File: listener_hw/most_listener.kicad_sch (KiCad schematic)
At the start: 121 parts, among them J1 1-1394640-1, J2 ANALYSER, J3 I2S, J4 VBAT_IN, J5 PLR135/T10, J6 PLT133/T10W, J7 RCA 75R, M1 Tang Nano 20K, M2 ESP32-DevKitC-VIE, U1 74LVC1G34, U10 TPS2553DBVR, U11 74LVC1G123, U12 DIR9001, U13 SRC4192, U14 LP5907MFX-3.3, U2 74LVC1G157, U3 74LVC1G125, U4 74LVC1G123, U5 TPS7B8133DRV, U6 LMR38020F, U7 Si514, U8 LP5907MFX-3.3, U9 74LVC1G79, X1 24.576MHz

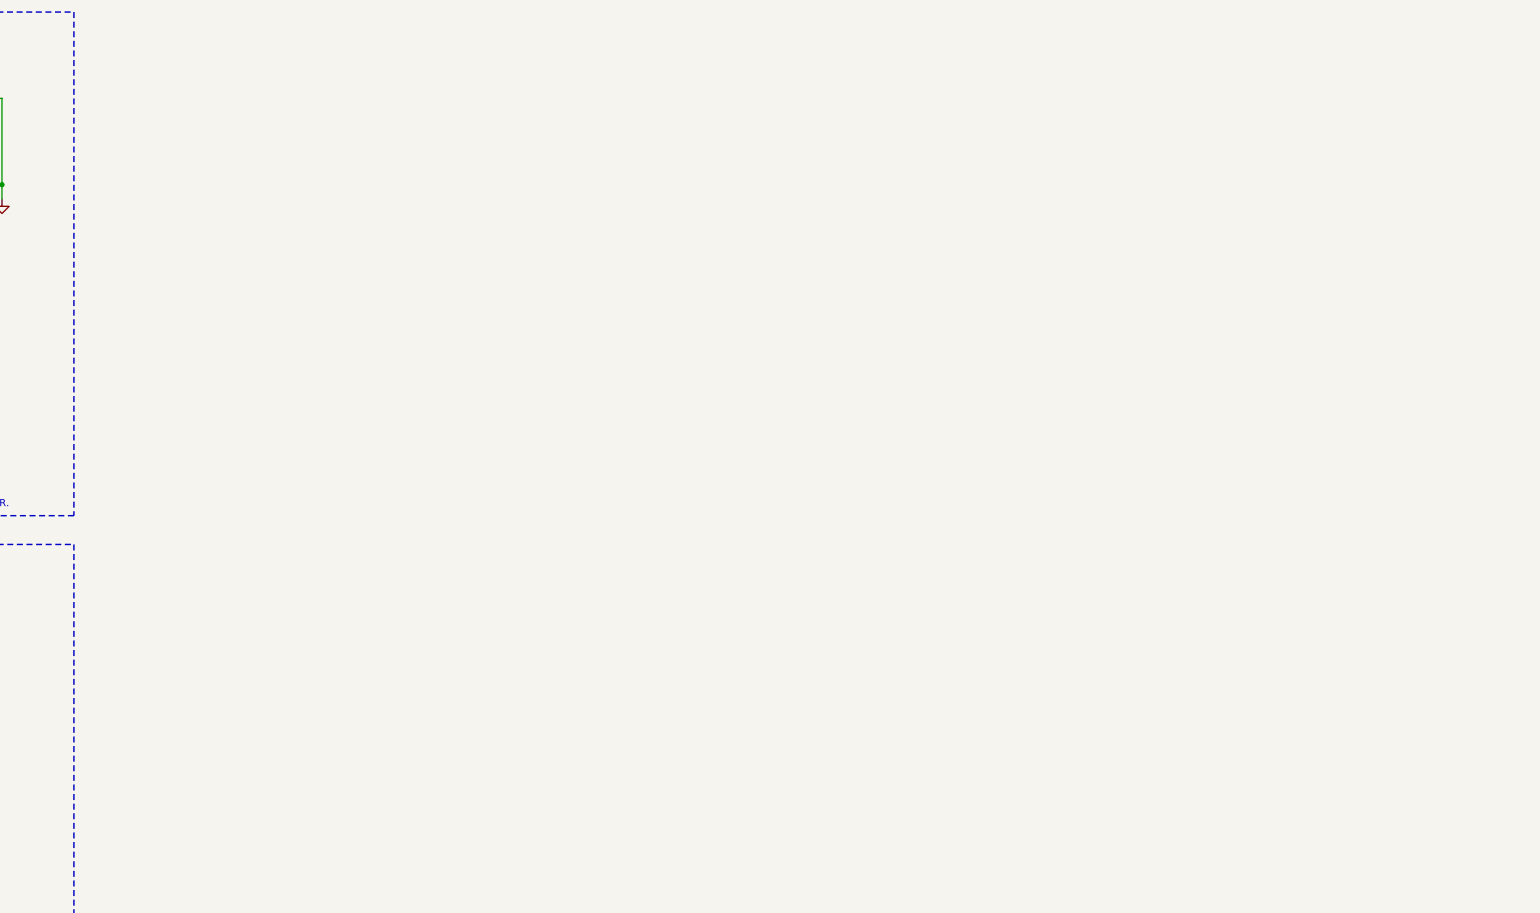
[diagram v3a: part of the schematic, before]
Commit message: Board: block 11, analog line out - PCM5102A on J3's stereo into the two RCA jacks placed by hand; footprints linked to the sheet
Sheet, block 11: U15 PCM5102A in hardware mode (FMT, FLT, DEMP low: I2S,
normal latency, no de-emphasis), SCK grounded so its PLL takes the clock from
BCK - three wires, the same I2S_BCLK_F / I2S_LRCK_F / I2S_DOUT_F that feed
J3 (64 Fs, 32-bit slots). XSMT from LOCK: muted while the ring is not locked
and while the FPGA is unconfigured (R8 holds LOCK low), with the chip's
104-sample soft ramp; no new FPGA pin, no gateware change. Outputs 2.1 Vrms
ground-centred through 470R + 2n2 C0G (TI SLAS859C Figure 33) to J8 (L) and
J9 (R), a PESD5V0S1BL at each jack as D4 at J7. U16, an LP5907, makes
3V3_DAC from 5V_SW; its output capacitance must stay within 10 uF (LP5907
data sheet), so AVDD gets 4.7 uF and CPVDD 2.2 uF instead of Figure 33's
10 uF each; LDOO 100n + 10u, flying cap and VNEG 2u2 each. Test points are
out of the BOM now (their footprints already said so). ERC clean.

Board: the placement the user reworked by hand since cddadba (the power
corner, block 9, J2/J3/U10 moved to the bottom middle, a fifth mounting hole
H5 at the top, two RCA jacks on the right edge copied from J7). The copies
became J9 (upper, right channel) and J8 (lower, left); block 11 sits in the
corner beside them, U15 turned so its analog pins face the jacks and its
digital pins face the I2S coming down from M2's pins. Every footprint now
carries its symbol's path and library name and single pins their
unconnected nets, the holes are board-only - DRC with --schematic-parity
finds no difference, so Update PCB from Schematic works from here. The
antenna keep-out is squared with M2 again. DRC: no error; the warnings are
silk, most of it in the hand-moved areas.

gen_listener_pcb.py writes the same links and parks parts its table does
not know beside the board instead of stopping. check_all.py's board step
also fails on any difference from the sheet. KiCad's local histor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
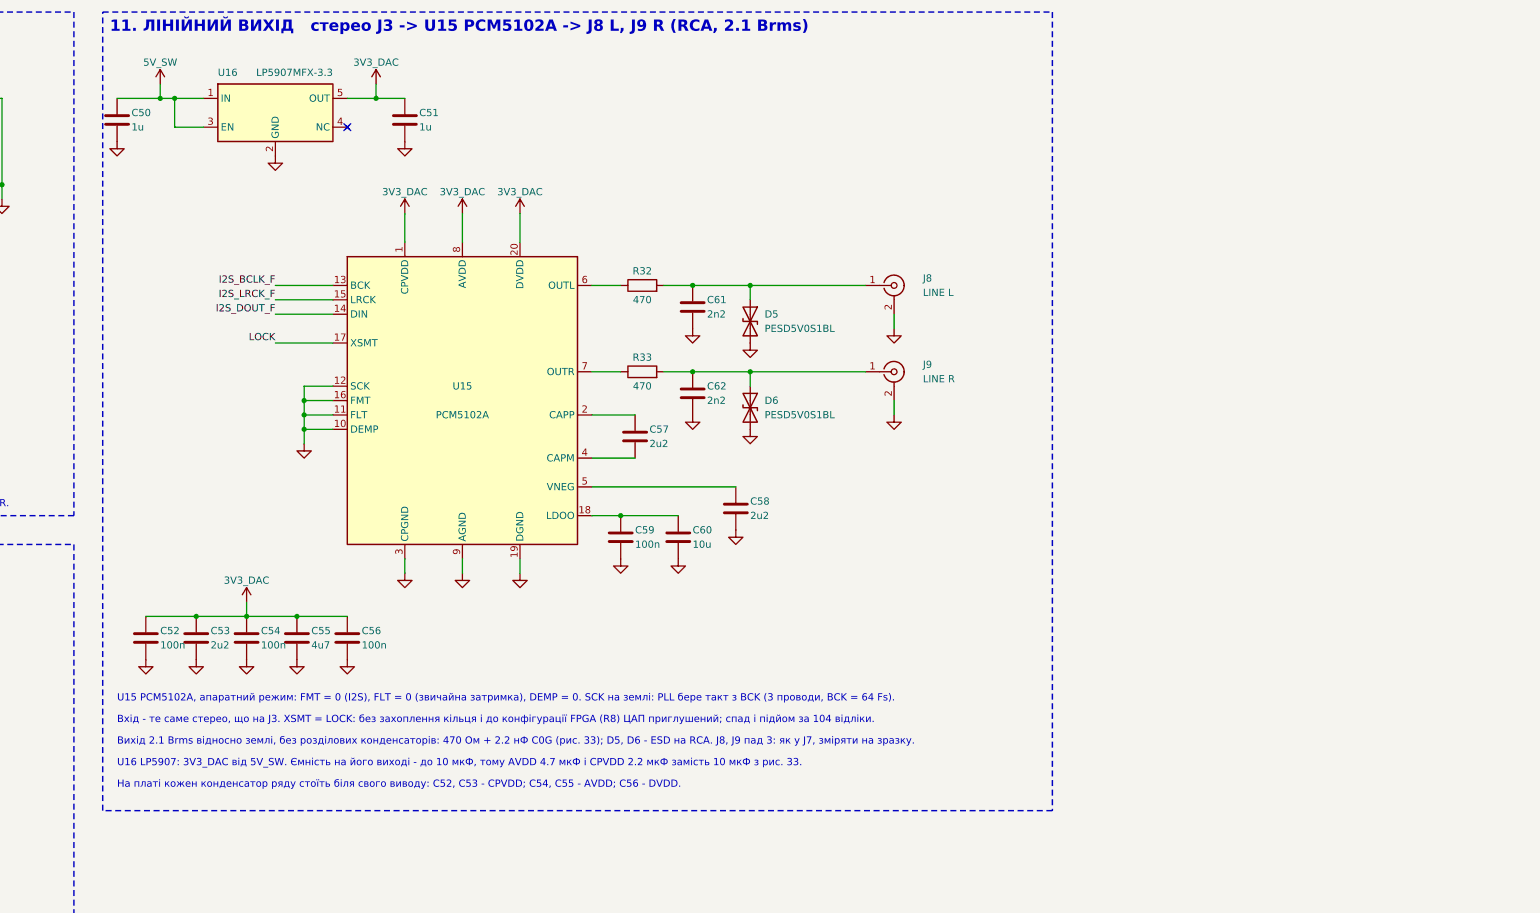
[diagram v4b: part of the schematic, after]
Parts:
- added C50, C51: 1u, Capacitor_SMD:C_0603_1608Metric, symbol Device:C
- added C52, C54, C56, C59: 100n, Capacitor_SMD:C_0603_1608Metric, symbol Device:C
- added C53, C57, C58: 2u2, Capacitor_SMD:C_0603_1608Metric, symbol Device:C
- added C55: 4u7, Capacitor_SMD:C_0805_2012Metric, symbol Device:C
- added C60: 10u, Capacitor_SMD:C_0805_2012Metric, symbol Device:C
- added C61, C62: 2n2, Capacitor_SMD:C_0603_1608Metric, symbol Device:C
- added D5, D6: PESD5V0S1BL, Diode_SMD:D_SOD-882, symbol Device:D_TVS
- added J8: LINE L, most_listener:BKL_0101153_RCA_RA, symbol Connector:Conn_Coaxial
- added J9: LINE R, most_listener:BKL_0101153_RCA_RA, symbol Connector:Conn_Coaxial
- added R32, R33: 470, Resistor_SMD:R_0603_1608Metric, symbol Device:R
- added U15: PCM5102A, Package_SO:TSSOP-20_4.4x6.5mm_P0.65mm, symbol most_listener:PCM5102A
- added U16: LP5907MFX-3.3, Package_TO_SOT_SMD:SOT-23-5, symbol most_listener:LP5907MFX-3.3
- TP1, TP2, TP3, TP4, TP5, TP6, TP7, TP8, TP9: now left out of the parts list
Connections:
- net 5V_SW: now also C50.1, U16.1 (IN), U16.3 (EN)
- net GND: now also C50.2, C51.2, C52.2, C53.2, C54.2, C55.2, C56.2, C58.2, C59.2, C60.2, C61.2, C62.2, D5.2 (A2), D6.2 (A2), J8.2 (Ext), J9.2 (Ext), U15.10 (DEMP), U15.11 (FLT), U15.12 (SCK), U15.16 (FMT), U15.19 (DGND), U15.3 (CPGND), U15.9 (AGND), U16.2 (GND)
- net I2S_BCLK_F: now also U15.13 (BCK)
- net I2S_DOUT_F: now also U15.14 (DIN)
- net I2S_LRCK_F: now also U15.15 (LRCK)
- net LOCK: now also U15.17 (XSMT)
- new net: C58.1, U15.5 (VNEG)
- new net: R33.1, U15.7 (OUTR)
- new net: C62.1, D6.1 (A1), J9.1 (In), R33.2
- new net: C59.1, C60.1, U15.18 (LDOO)
- new net: C61.1, D5.1 (A1), J8.1 (In), R32.2
- new net: C57.1, U15.2 (CAPP)
- new net: C57.2, U15.4 (CAPM)
- new net: R32.1, U15.6 (OUTL)
- new net 3V3_DAC: C51.1, C52.1, C53.1, C54.1, C55.1, C56.1, U15.1 (CPVDD), U15.20 (DVDD), U15.8 (AVDD), U16.5 (OUT)
- no-connect marks 62 -> 63
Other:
- note added: "11. ЛІНІЙНИЙ ВИХІД стерео J3 -> U15 PCM5102A -> J8 L, J9 R (RCA, 2.1 Вrms)"
- note added: "U15 PCM5102A, апаратний режим: FMT = 0 (I2S), FLT = 0 (звичайна затримка), DEMP = 0. SCK на землі: PLL бере такт з BCK (3 проводи, BCK = 64 Fs)."
- note added: "U16 LP5907: 3V3_DAC від 5V_SW. Ємність на його виході - до 10 мкФ, тому AVDD 4.7 мкФ і CPVDD 2.2 мкФ замість 10 мкФ з рис. 33."
- note added: "Вихід 2.1 Вrms відносно землі, без розділових конденсаторів: 470 Ом + 2.2 нФ C0G (рис. 33); D5, D6 - ESD на RCA. J8, J9 пад 3: як у J7, зміряти на зразку."
- note added: "Вхід - те саме стерео, що на J3. XSMT = LOCK: без захоплення кільця і до конфігурації FPGA (R8) ЦАП приглушений; спад і підйом за 104 відліки."
- note added: "На платі кожен конденсатор ряду стоїть біля свого виводу: C52, C53 - CPVDD; C54, C55 - AVDD; C56 - DVDD."

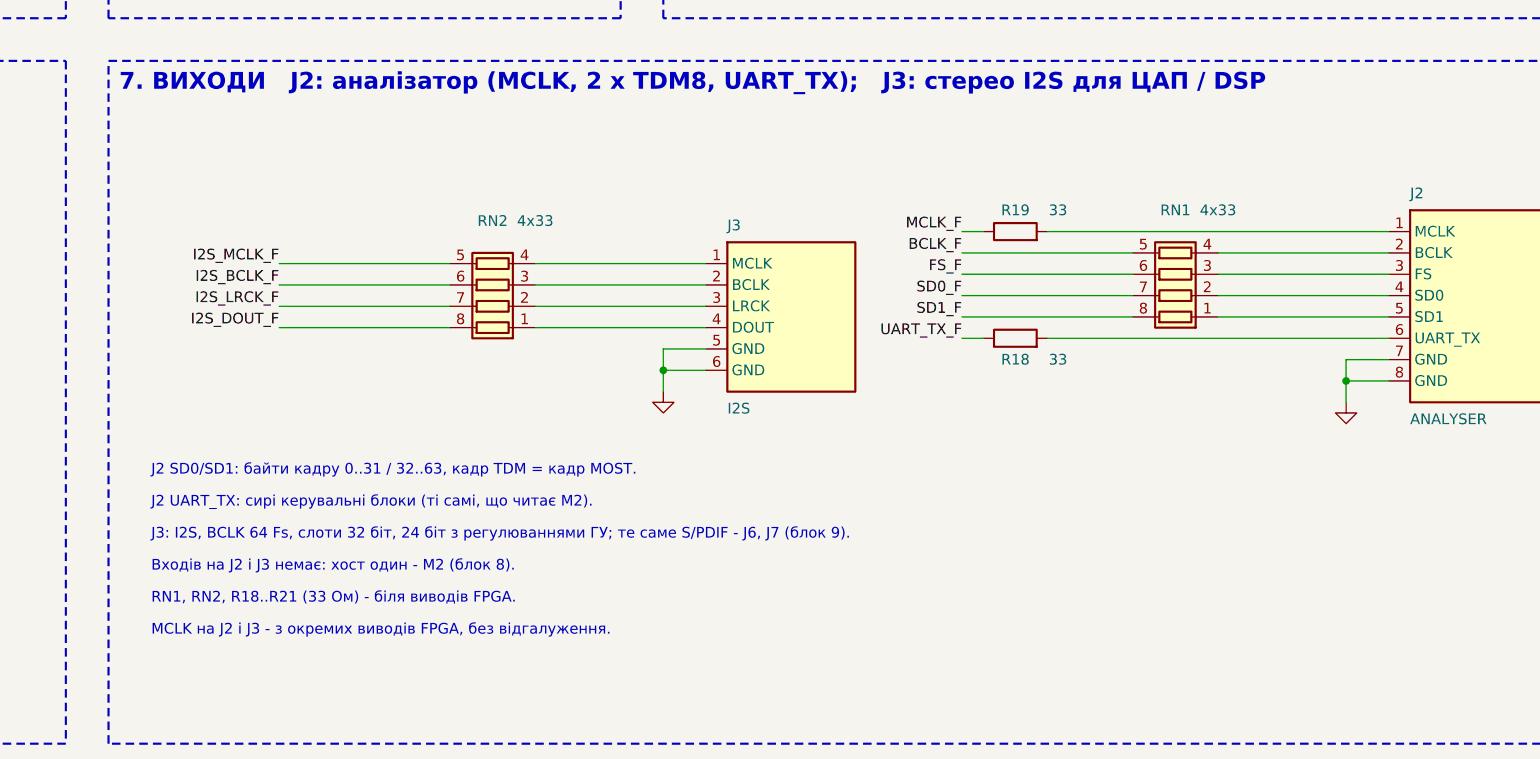
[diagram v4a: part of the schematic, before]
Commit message: Board: the user's regroup, reviewed - 33R singles under M1 at their FPGA pins, U14 back in block 9, block 9 turned to its jacks, the capacitor copies out
The user regrouped the board: M2 upright against M1 with both USB ends at
the top edge, every audio jack (TOSLINK in and out, coax, the two line-out
RCA) on the right edge, block 9 beside them, the host switch and the test
points in the bottom middle, a sixth mounting hole (H6) on the left edge.
Agreed after review and done here:

- Sheet: RN1 and RN2 (4 x 33R arrays) became single 0603 resistors, R34..R41,
  so each FPGA output to J2/J3 has its own. With R18..R21 they sit under M1,
  each beside its FPGA pin (source termination: MCLK, BCLK and TDM lines run
  to the headers and on through cables). The Tang Nano's footprint now keeps
  only its two socket rows as courtyard, so low parts may sit under the
  module standing on its 8.5 mm sockets; its outline stays on fab and silk.
  R20 had landed on M2's pins 37/38 (the seven DRC errors of the regroup);
  it sits at M1 pin 1 now. ERC clean.
- U14 with C48/C49 back in block 9: the clean 3V3_DA stays short, the long
  run is 5V_SW's.
- Block 9 re-laid for the jacks on the right edge: DIR9001 next to J5 with
  RXIN and its loop filter towards the jack, SRC4192 between it and the
  modules with its I2S outputs towards them, X1 at RCKI, FB3/C30 within 2 cm
  of J5 as the Everlight sheet asks, C31 by J6, the coax divider and D4 by J7.
- The three board-only copies each of C45 and C47 are gone: two 100 uF
  pairs are what the input needs; more only raises the inrush through F1.
- Both antenna keep-outs squared with M2 upright (the B.Cu one was half
  height); C61/D5 and C62/D6 moved up with J8/J9.

DRC: no error; 368 unconnected (not routed); the warnings are silk, for the
final silk pass. DRC with --schematic-parity: no difference. The board
generator's table lost RN1/RN2; a fresh layout parks the parts it does not
know beside the board and still matches the sheet.

Co-Au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
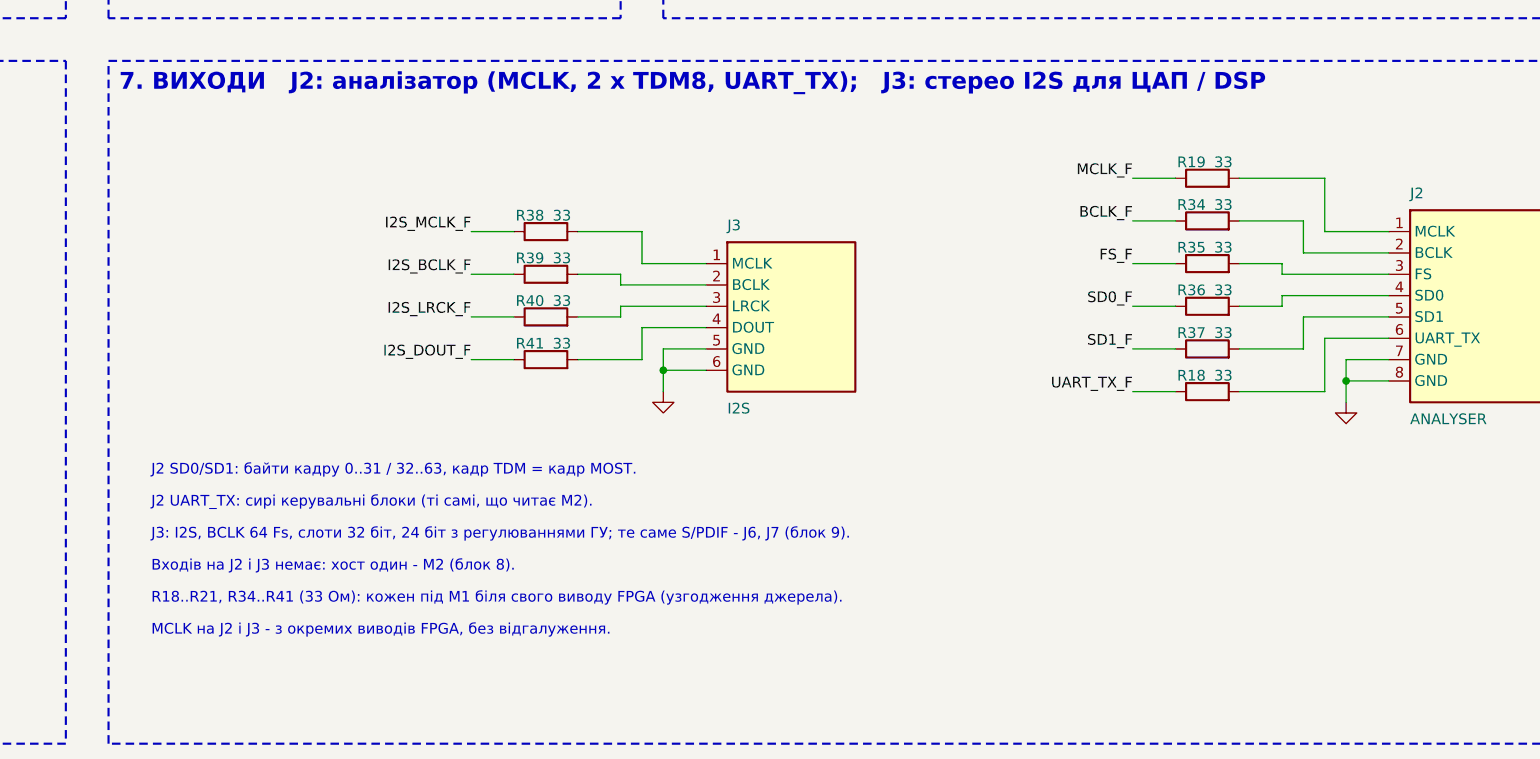
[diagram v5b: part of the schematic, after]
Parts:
- removed RN1, RN2: 4x33, Resistor_SMD:R_Array_Convex_4x0603, symbol Device:R_Pack04
- added R34, R35, R36, R37, R38, R39, R40, R41: 33, Resistor_SMD:R_0603_1608Metric, symbol Device:R
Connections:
- net BCLK_F: now also R34.1
- net FS_F: now also R35.1
- net I2S_BCLK_F: now also R39.1
- net I2S_DOUT_F: now also R41.1
- net I2S_LRCK_F: now also R40.1
- net I2S_MCLK_F: now also R38.1
- net SD0_F: now also R36.1
- net SD1_F: now also R37.1
- net at J3.1 (MCLK): now also R38.2
- net at J3.2 (BCLK): now also R39.2
- net at J3.3 (LRCK): now also R40.2
- net at J3.4 (DOUT): now also R41.2
- net at J2.5 (SD1): now also R37.2
- net at J2.4 (SD0): now also R36.2
- net at J2.3 (FS): now also R35.2
- net at J2.2 (BCLK): now also R34.2
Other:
- note added: "R18..R21, R34..R41 (33 Ом): кожен під M1 біля свого виводу FPGA (узгодження джерела)."
- note removed: "RN1, RN2, R18..R21 (33 Ом) - біля виводів FPGA."
- moved on the sheet: R18, R19

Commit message: Board: M1 and M2 left into the strip the user freed; resistors of M1's pins under it; signal test points above J1
The user cleared a vertical strip left of M1 and asked for the FPGA to move
into it, part of the resistors to go under the module, and the signal test
points to go to the left edge above the MOST header.

- The ring-logic column (U3, U9, R16) with R17 moved into the strip; M1
  followed it 6.7 mm to the left and M2 with M1, the two modules still side
  by side; the antenna keep-out moved with M2. The free space now lies
  between M2 and block 9, a channel for M2's signals to the right half.
- Under M1, each beside its pin, as before for J2/J3's 33R: R20 (pin 1,
  UART_RX_F), R14 (pin 5, CLK_1024's pull-down), R11/R12 (pins 12/13, the
  Si514 I2C pull-ups). R10, the 22R source termination of the Si514's
  output, went to the Si514 next to R15, not to the FPGA end.
- Parts left behind by the regroup rejoined their chips: U11's timing RC
  (R23, C25) and decoupling (C26) at U11, C14 at U8's output.
- The signal test points RX_BUF, TX_REGEN, TX_SEL, WAKE, RT_CLK sit in a
  block above J1 with two ground points beside them: TP8 and TP10, the copy
  of TP8 the user had made, now its own part in the sheet (block 10). TP7
  (5V_SW) came out from under M1's HDMI connector.

ERC clean; DRC: no error, no difference from the sheet; the warnings are
silk, for the final silk pass. The board generator tolerates test points
its table does not know (TP10).

Co-Authored-By: Claude Opus 5.5 <noreply@anthropic.com>
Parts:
- added TP10: GND, TestPoint:TestPoint_Pad_D2.0mm, symbol Connector:TestPoint
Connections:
- net GND: now also TP10.1
